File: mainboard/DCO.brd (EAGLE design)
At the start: 59.4 x 23 mm, 44 parts, among them IC101 LF353D, IC201 LF353D, P101 TRIMPOT 100K, U1 XMEGA-A4VQFN

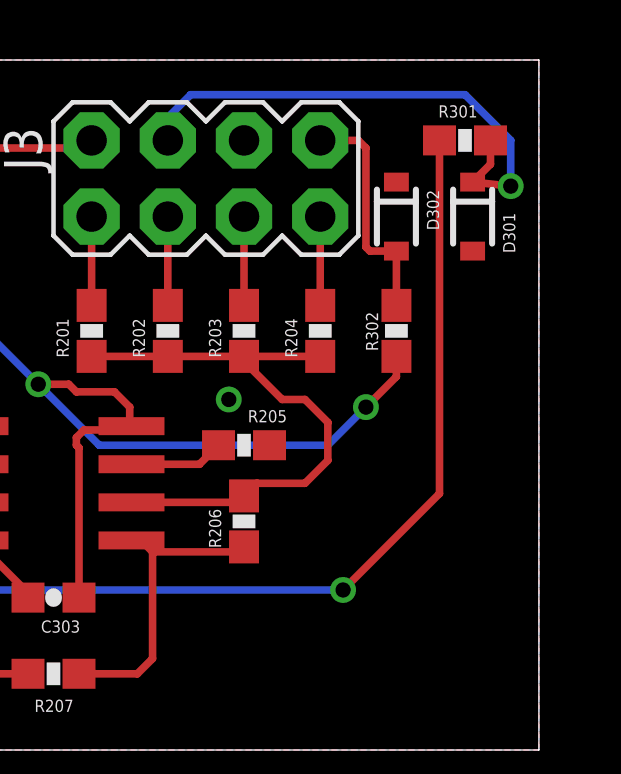
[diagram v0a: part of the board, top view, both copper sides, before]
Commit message: adjusted labels on bottom of board
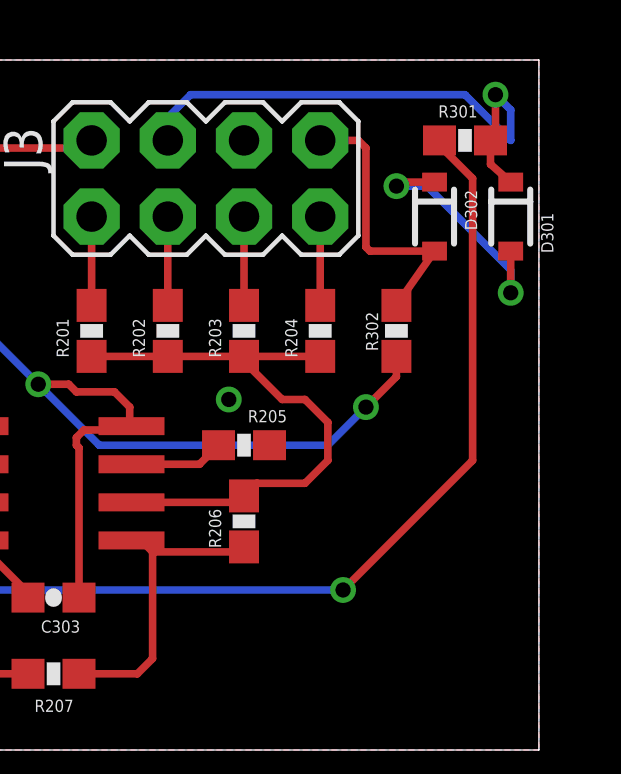
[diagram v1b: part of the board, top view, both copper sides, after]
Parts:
- added U$1: (no value), SparkFun:OSHW-LOGO-L
- moved D301 1.27 mm to (58.4, 17.8)
- moved D302 1.27 mm to (55.9, 17.8)
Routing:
- net GND: track 14.5 -> 22.8 mm, vias 3 -> 5
- net -5V: track 7.81 -> 9.48 mm
- net +12V: track 122.6 -> 123.5 mm
- net +5V: track 17.6 -> 18.2 mm
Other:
- board text added: "Alpha"
- board text added: "Computer"
- board text added: "Controlled"
- board text added: "Oscillator"
- board text added: "Output Gain Adj."
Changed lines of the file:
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@@
 <layer number="23" name="tOrigins" color="15" fill="1" visible="yes" active="yes"/>
 <layer number="24" name="bOrigins" color="15" fill="1" visible="yes" active="yes"/>
-<layer number="25" name="tNames" color="7" fill="1" visible="yes" active="yes"/>
-<layer number="26" name="bNames" color="7" fill="1" visible="yes" active="yes"/>
+<layer number="25" name="tNames" color="7" fill="1" visible="no" active="yes"/>
+<layer number="26" name="bNames" color="7" fill="1" visible="no" active="yes"/>
 <layer number="27" name="tValues" color="7" fill="1" visible="no" active="yes"/>
 <layer number="28" name="bValues" color="7" fill="1" visible="no" active="yes"/>
@@
 <wire x1="59.36" y1="23" x2="0" y2="23" width="0" layer="20"/>
 <wire x1="0" y1="23" x2="0" y2="0" width="0" layer="20"/>
+<text x="58.42" y="8.636" size="1.6764" layer="22" font="vector" ratio="15" rot="MR0">Computer</text>
+<text x="58.42" y="6.35" size="1.6764" layer="22" font="vector" ratio="15" rot="MR0">Controlled</text>
+<text x="58.42" y="4.318" size="1.6764" layer="22" font="vector" ratio="15" rot="MR0">Oscillator</text>
+<text x="52.832" y="2.286" size="1.6764" layer="22" font="vector" ratio="15" rot="MR0">Alpha</text>
+<text x="42.926" y="12.7" size="1.27" layer="22" font="vector" ratio="15" rot="MR0">Output Gain Adj.</text>
+<wire x1="23.114" y1="10.16" x2="24.13" y2="9.144" width="0.254" layer="22"/>
+<wire x1="24.13" y1="9.144" x2="25.146" y2="10.16" width="0.254" layer="22"/>
 </plain>
 <attributes>
@@
 <element name="R110" library="SparkFun" package="0603-RES" value="1K" x="38.1" y="12.7" rot="R270"/>
 <element name="P101" library="SparkFun" package="TRIM_POT_PTH" value="TRIMPOT 100K" x="36.88" y="17.95" smashed="yes" rot="MR90">
-<attribute name="NAME" x="33.578" y="17.569" size="0.6096" layer="26" rot="MR90"/>
+<attribute name="NAME" x="33.578" y="17.315" size="0.6096" layer="26" rot="MR90"/>
 <attribute name="VALUE" x="36.88" y="21.125" size="0.6096" layer="28" rot="MR90"/>
 </element>
-<element name="TP101" library="SparkFun" package="1X01" value="" x="12.7" y="20.32" rot="MR0"/>
-<element name="TP102" library="SparkFun" package="1X01" value="" x="22.86" y="20.32" rot="MR0"/>
-<element name="TP104" library="SparkFun" package="1X01" value="" x="26.67" y="5.08" rot="MR0"/>
-<element name="TP103" library="SparkFun" package="1X01" value="" x="19.05" y="11.43" rot="MR0"/>
+<element name="TP101" library="SparkFun" package="1X01" value="" x="12.7" y="20.32" smashed="yes" rot="MR0">
+<attribute name="NAME" x="15.3162" y="17.5768" size="1.27" layer="26" rot="MR0"/>
+<attribute name="VALUE" x="13.97" y="17.145" size="1.27" layer="28" rot="MR0"/>
+</element>
+<element name="TP102" library="SparkFun" package="1X01" value="" x="22.86" y="20.32" smashed="yes" rot="MR0">
+<attribute name="NAME" x="24.7142" y="17.5768" size="1.27" layer="26" rot="MR0"/>
+<attribute name="VALUE" x="24.13" y="17.145" size="1.27" layer="28" rot="MR0"/>
+</element>
+<element name="TP104" library="SparkFun" package="1X01" value="" x="26.67" y="5.08" smashed="yes" rot="MR0">
+<attribute name="NAME" x="31.5722" y="6.6548" size="1.27" layer="26" rot="MR0"/>
+<attribute name="VALUE" x="27.94" y="1.905" size="1.27" layer="28" rot="MR0"/>
+</element>
+<element name="TP103" library="SparkFun" package="1X01" value="" x="19.05" y="11.43" smashed="yes" rot="MR0">
+<attribute name="NAME" x="17.0942" y="10.9728" size="1.27" layer="26" rot="MR0"/>
+<attribute name="VALUE" x="20.32" y="8.255" size="1.27" layer="28" rot="MR0"/>
+</element>
 <element name="R101" library="SparkFun" package="0603-RES" value="10K" x="15.24" y="20.32" rot="R90"/>
 <element name="IC101" library="linear" package="SO08" value="LF353D" x="29.21" y="13.97"/>
@@
 <element name="C302" library="SparkFun" package="0603-CAP" value=".1uF" x="33.02" y="12.7" rot="R90"/>
 <element name="C303" library="SparkFun" package="0603-CAP" value=".1uF" x="43.18" y="5.08" rot="R180"/>
-<element name="D301" library="SparkFun" package="SOD-323" value="5V" x="57.15" y="17.78" smashed="yes" rot="R270">
-<attribute name="NAME" x="58.166" y="17.907" size="0.4064" layer="25" rot="R270"/>
-<attribute name="VALUE" x="55.753" y="18.796" size="0.4064" layer="27" rot="R270"/>
-</element>
-<element name="D302" library="SparkFun" package="SOD-323" value="5V" x="54.61" y="17.78" rot="R270"/>
+<element name="D301" library="SparkFun" package="SOD-323" value="5V" x="58.42" y="17.78" smashed="yes" rot="R270">
+<attribute name="NAME" x="59.436" y="17.907" size="0.4064" layer="25" rot="R270"/>
+<attribute name="VALUE" x="57.023" y="18.796" size="0.4064" layer="27" rot="R270"/>
+</element>
+<element name="D302" library="SparkFun" package="SOD-323" value="5V" x="55.88" y="17.78" rot="R270"/>
 <element name="R301" library="SparkFun" package="0603-RES" value="100K" x="56.896" y="20.32"/>
 <element name="R302" library="SparkFun" package="0603-RES" value="100K" x="54.61" y="13.97" smashed="yes" rot="R270">
@@
 <attribute name="VALUE" x="6.477" y="16.256" size="0.4064" layer="27" font="vector" rot="R270"/>
 </element>
-<element name="H1" library="Batten" package="AVR_ISP_6" value="PDI" x="22.86" y="5.08" rot="MR0"/>
-<element name="POWER" library="eurorack" package="POWER_16" value="POWER_SIMPLE16" x="3.81" y="13.97" rot="MR270"/>
+<element name="H1" library="Batten" package="AVR_ISP_6" value="PDI" x="22.86" y="5.08" smashed="yes" rot="MR0"/>
+<element name="POWER" library="eurorack" package="POWER_16" value="POWER_SIMPLE16" x="3.81" y="13.97" smashed="yes" rot="MR270">
+<attribute name="NAME" x="8.255" y="7.874" size="1.27" layer="26" ratio="10" rot="MR270"/>
+</element>
 <element name="J3" library="SparkFun" package="2X4" value="" x="48.26" y="19.05" smashed="yes">
 <attribute name="NAME" x="42.799" y="19.304" size="1.27" layer="25" ratio="10" rot="R90"/>
@@
 </element>
 <element name="C304" library="SparkFun" package="1206" value="10uF" x="17.78" y="6.35" rot="R270"/>
+<element name="U$1" library="SparkFun" package="OSHW-LOGO-L" value="" x="55.626" y="13.462" rot="MR0"/>
 </elements>
 <signals>
@@
 <via x="39.624" y="21.336" extent="1-16" drill="0.508"/>
 <via x="7.874" y="17.526" extent="1-16" drill="0.508"/>
+<wire x1="55.88" y1="18.93" x2="54.744" y2="18.93" width="0.254" layer="1"/>
+<wire x1="54.744" y1="18.93" x2="54.61" y2="18.796" width="0.254" layer="1"/>
+<via x="54.61" y="18.796" extent="1-16" drill="0.508"/>
+<wire x1="54.61" y1="18.796" x2="55.626" y2="18.796" width="0.254" layer="16"/>
+<wire x1="55.626" y1="18.796" x2="58.42" y2="16.002" width="0.254" layer="16"/>
+<wire x1="58.42" y1="16.002" x2="58.42" y2="15.24" width="0.254" layer="16"/>
+<via x="58.42" y="15.24" extent="1-16" drill="0.508"/>
+<wire x1="58.42" y1="15.24" x2="58.42" y2="16.51" width="0.254" layer="1"/>
 </signal>
 <signal name="N$7">
@@
 <contactref element="J3" pad="4"/>
 <wire x1="57.746" y1="20.32" x2="57.746" y2="19.526" width="0.254" layer="1"/>
-<wire x1="57.746" y1="19.526" x2="57.15" y2="18.93" width="0.254" layer="1"/>
-<wire x1="57.15" y1="18.93" x2="58.42" y2="18.796" width="0.254" layer="1"/>
-<via x="58.42" y="18.796" extent="1-16" drill="0.508"/>
-<wire x1="58.42" y1="18.796" x2="58.42" y2="20.32" width="0.254" layer="16"/>
+<wire x1="57.746" y1="19.526" x2="58.42" y2="18.93" width="0.254" layer="1"/>
 <wire x1="58.42" y1="20.32" x2="56.896" y2="21.844" width="0.254" layer="16"/>
 <wire x1="56.896" y1="21.844" x2="47.752" y2="21.844" width="0.254" layer="16"/>
 <wire x1="47.752" y1="21.844" x2="46.99" y2="21.082" width="0.254" layer="16"/>
 <wire x1="46.99" y1="21.082" x2="46.99" y2="20.32" width="0.254" layer="16"/>
+<wire x1="58.42" y1="20.32" x2="58.42" y2="21.336" width="0.254" layer="16"/>
+<wire x1="58.42" y1="21.336" x2="57.912" y2="21.844" width="0.254" layer="16"/>
+<via x="57.912" y="21.844" extent="1-16" drill="0.508"/>
+<wire x1="57.912" y1="21.844" x2="57.912" y2="20.486" width="0.254" layer="1"/>
+<wire x1="57.912" y1="20.486" x2="57.746" y2="20.32" width="0.254" layer="1"/>
 </signal>
 <signal name="-5V">
@@
 <contactref element="D302" pad="2"/>
 <contactref element="R302" pad="1"/>
-<wire x1="54.61" y1="14.82" x2="54.61" y2="16.63" width="0.254" layer="1"/>
-<wire x1="54.61" y1="16.63" x2="53.728" y2="16.63" width="0.254" layer="1"/>
+<wire x1="54.61" y1="14.82" x2="55.88" y2="16.63" width="0.254" layer="1"/>
+<wire x1="55.88" y1="16.63" x2="53.728" y2="16.63" width="0.254" layer="1"/>
 <wire x1="53.728" y1="16.63" x2="53.594" y2="16.764" width="0.254" layer="1"/>
 <wire x1="53.594" y1="16.764" x2="53.594" y2="20.066" width="0.254" layer="1"/>
@@
 <wire x1="16.6514" y1="0.9034" x2="14.986" y2="1.016" width="0.254" layer="1"/>
 <via x="14.986" y="1.016" extent="1-16" drill="0.508"/>
-<wire x1="56.046" y1="20.32" x2="56.046" y2="8.548" width="0.254" layer="1"/>
-<wire x1="56.046" y1="8.548" x2="52.832" y2="5.334" width="0.254" layer="1"/>
+<wire x1="57.15" y1="9.652" x2="52.832" y2="5.334" width="0.254" layer="1"/>
 <via x="52.832" y="5.334" extent="1-16" drill="0.508"/>
 <wire x1="52.832" y1="5.334" x2="40.386" y2="5.334" width="0.254" layer="16"/>
@@
 <wire x1="14.986" y1="1.016" x2="15.24" y2="0.762" width="0.254" layer="16"/>
 <wire x1="15.24" y1="0.762" x2="30.734" y2="0.762" width="0.254" layer="16"/>
+<wire x1="56.046" y1="20.32" x2="56.046" y2="20.154" width="0.254" layer="1"/>
+<wire x1="56.046" y1="20.154" x2="57.15" y2="19.05" width="0.254" layer="1"/>
+<wire x1="57.15" y1="19.05" x2="57.15" y2="9.652" width="0.254" layer="1"/>
 </signal>
 <signal name="+3V3">
